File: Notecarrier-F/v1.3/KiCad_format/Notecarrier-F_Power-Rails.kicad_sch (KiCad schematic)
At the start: 31 parts, among them U3 TPS63020DSJR, U7 MAX17225ELT+, U8 TPS62748YFPT, U9 AP2139AK-3.3TRG1

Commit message: kicad_validation: make the BOM and placement gates actually gate
Two of the three proof gates could not fail on the thing they claimed to check.

BOM: the MPN comparison was guarded on `k["mpn"]` being non-empty, so a released
BOM naming a part and a KiCad symbol carrying no MPN at all compared equal and
reported "PASS - BOM matches exactly". Missing data was being read as agreement.
Value and MPN were also chained with elif, so an MPN mismatch was hidden behind
a value mismatch on the same refdes. Both fixed, and a blank KiCad MPN now fails
whenever the shipped BOM has one.

That immediately caught real data loss: C33 and C34, added to Notecarrier-F
earlier on this branch, had no MPN. Set to CC0603KRX5R8BB105 / Yageo per
BOM-3000-653-002. J11 is the only remaining blank and it is DNP, so excluded.

Placement: the gate computed position residuals and then omitted them from the
verdict, so a footprint could move anywhere and still pass - and
allowed_position_outliers was configured for X and XS but read by no code.

Rather than bless the residuals with a hand-kept table, each part's expected
residual is now predicted from its own pad bounding box, since the assembly file
references the body centre while KiCad measures from the footprint origin. That
explains almost everything outright: Notecarrier-XI's P1/P2 sit 19.05mm out
because their footprint - named "1X16" - has its origin on pad 1 of a 38.1mm
header, which is exactly half its length.

What the prediction cannot explain must be listed in a committed
placement-baseline.yaml, so it is reviewed once and then frozen against drift.
The 12 entries across five boards are all 0.3-0.7mm on JST connectors with a
plastic shroud wider than their pads, and on diodes whose large tab pad pulls
the pad bounding box off the package centre. allowed_position_outliers is gone,
superseded by that file.

Verified by nudging one Notecarrier-XM footprint 1mm: the gate now fails it.
All five configured boards pass with their baselines 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
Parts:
- C33, C34: MPN (none) -> CC0603KRX5R8BB105; Manufacturer (none) -> Yageo
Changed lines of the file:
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@@
+			)
+		)
+		(property "MPN" "CC0603KRX5R8BB105"
+			(at 203.2 33.02 0)
+			(effects
+				(font
+					(size 1.27 1.27)
+				)
+				(hide yes)
+			)
+		)
+		(property "Manufacturer" "Yageo"
+			(at 203.2 33.02 0)
+			(effects
+				(font
+					(size 1.27 1.27)
+				)
+				(hide yes)
 			)
 		)
@@
 			)
 		)
+		(property "MPN" "CC0603KRX5R8BB105"
+			(at 226.06 33.02 0)
+			(effects
+				(font
+					(size 1.27 1.27)
+				)
+				(hide yes)
+			)
+		)
+		(property "Manufacturer" "Yageo"
+			(at 226.06 33.02 0)
+			(effects
+				(font
+					(size 1.27 1.27)
+				)
+				(hide yes)
+			)
+		)

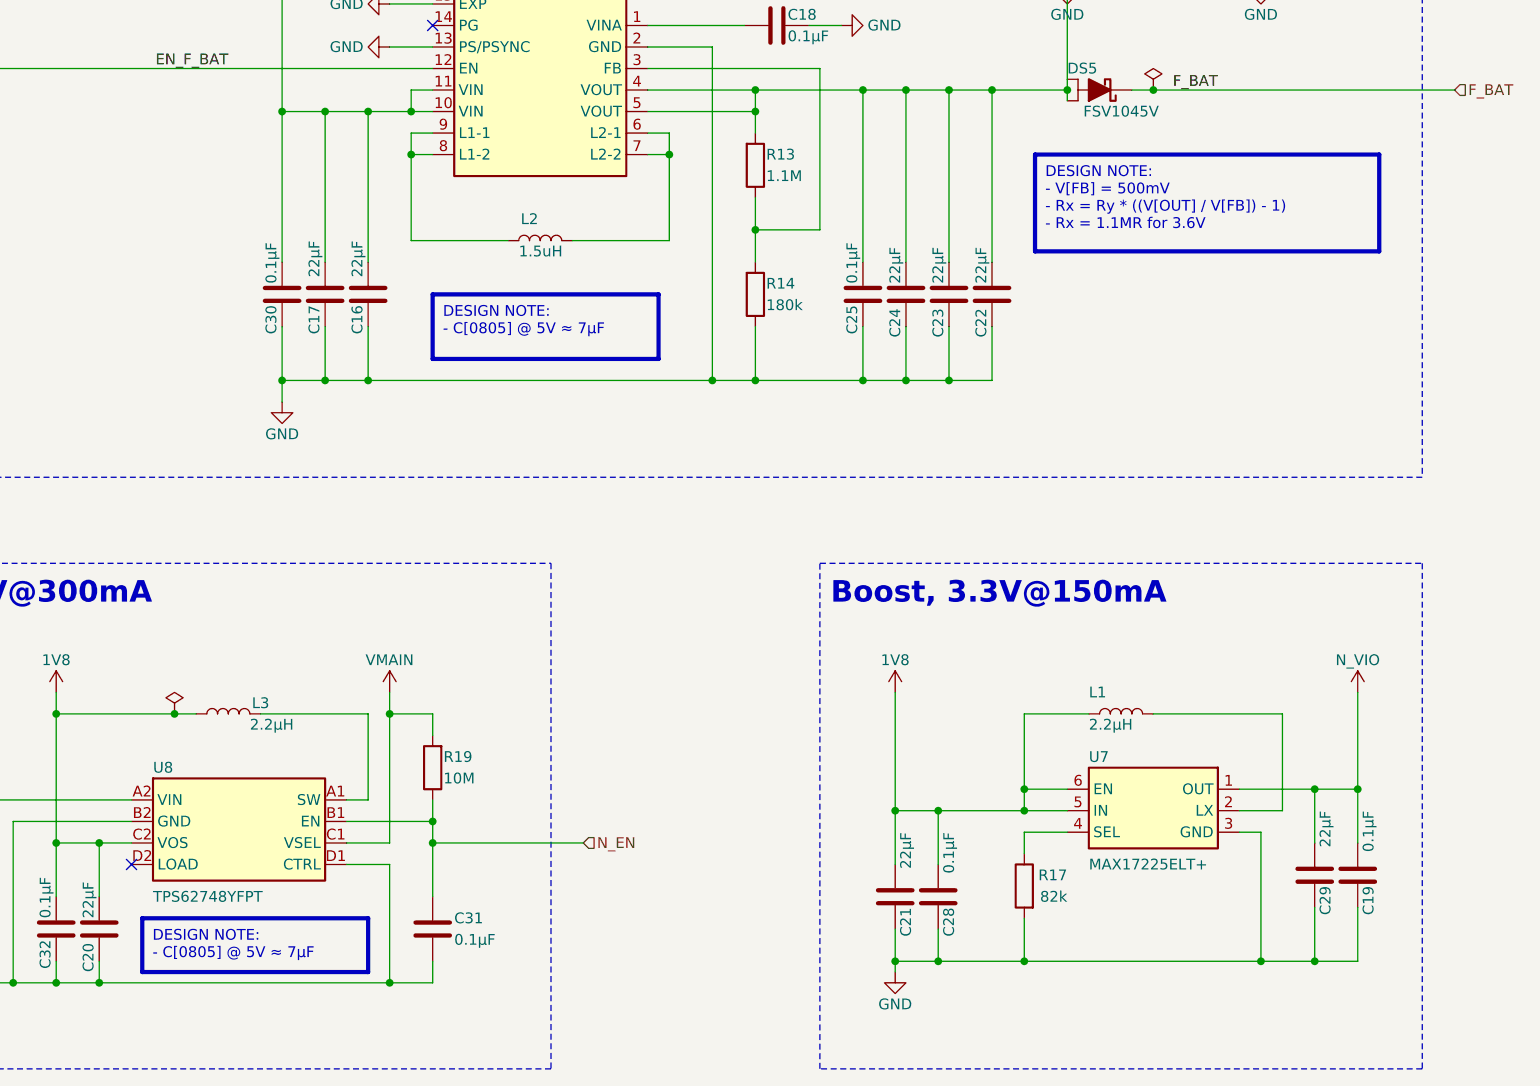
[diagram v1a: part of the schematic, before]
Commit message: Notecarrier-F: convert its design-note text_boxes too
The first conversion pass scoped by red-frame rectangles and missed
Notecarrier-F: its 16 notes have no separate frame - the text_box itself draws
a 0.5mm red border - so they were entirely invisible on the published pages,
frames included. Same conversion as 25a2d84, with two additions the F notes
forced:

- KiCad's hidden PDF text layer mangles special glyphs (broken ToUnicode maps
  for u/~/ohm produce mojibake) and F's notes are full of them, so exact
  word-matching is unattainable. Notes whose visual line count matches their
  source line count need no wrap-freezing at all and are kept verbatim, guarded
  by a per-line ASCII similarity check; only genuinely wrapped notes use the
  strict word-level path, and F's wrapped notes are clean of special glyphs.
  The converter also now rebuilds output from SOURCE words - the PDF only
  supplies break positions - so KiCad markup like R_{iset} stays markup in the
  file instead of being replaced by its rendered form.

- The F author gave these notes an explicit black font color. Black is what
  KiCad plots either way, but explicit black is invisible on a dark-theme
  viewer. The 16 notes now carry no explicit color, like every other board's
  notes: KiCad plots its default dark blue, kicanvas its theme color. This is
  the one deliberate visual change - note text black -> dark blue in KiCad -
  and it makes F consistent with the other five boards.

Netlist byte-equal before and after; kicanvas renders all four modified sheets
with the notes visible and the subscript markup intact.

Co-Authored-By: Claude Fable 5 <noreply@anthropic.com>
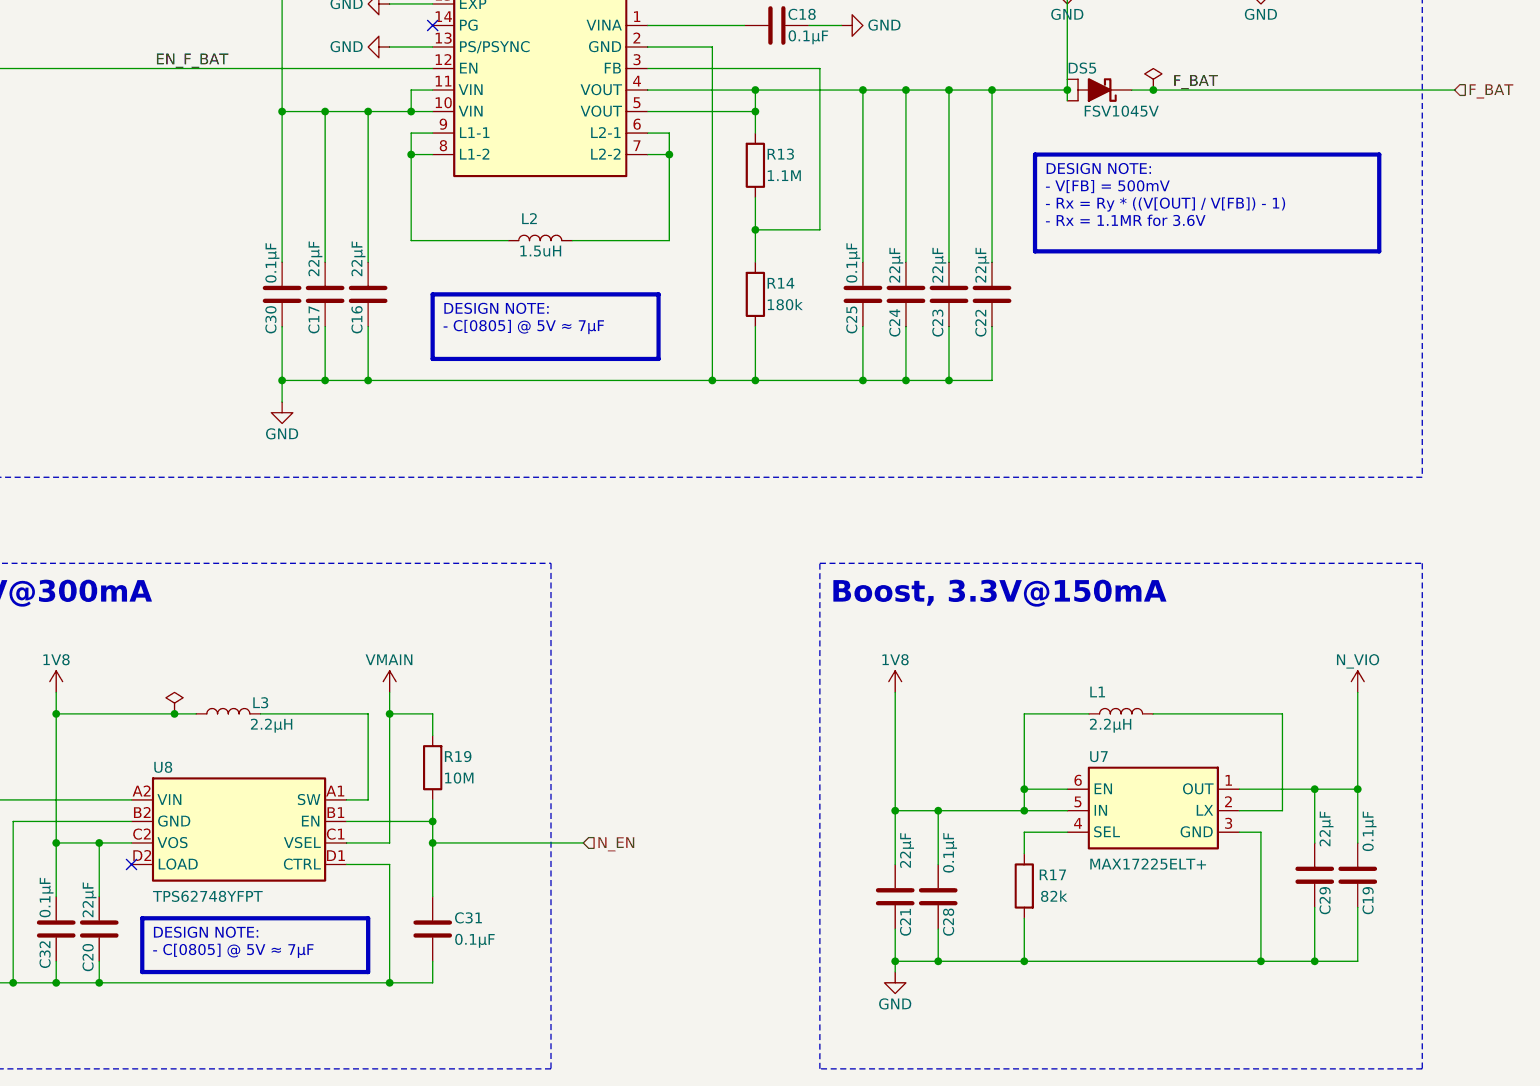
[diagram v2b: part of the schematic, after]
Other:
- note added: "DESIGN NOTE: - C[0805] @ 5V ≈ 7µF"
- note added: "DESIGN NOTE: - V[FB] = 500mV - Rx = Ry * ((V[OUT] / V[FB]) - 1) - Rx = 1.1MR for 3.6V"
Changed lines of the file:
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@@
 		)
 	)
-	(text_box "DESIGN NOTE:\n- C[0805] @ 5V ≈ 7µF"
-		(exclude_from_sim no)
-		(at 128.27 73.66 0)
-		(size 26.67 7.62)
-		(margins 1.2025 1.2025 1.2025 1.2025)
+	(rectangle
+		(start 128.27 73.66)
+		(end 154.94 81.28)
 		(stroke
 			(width 0.5)
@@
 			(type none)
 		)
+	)
+	(text "DESIGN NOTE:\n- C[0805] @ 5V ≈ 7µF"
+		(exclude_from_sim no)
+		(at 129.472 74.8625 0)
 		(effects
 			(font
 				(size 1.27 1.27)
-				(color 0 0 0 1)
 			)
 			(justify left top)
 		)
 	)
-	(text_box "DESIGN NOTE:\n- C[0805] @ 5V ≈ 7µF"
-		(exclude_from_sim no)
-		(at 93.98 147.32 0)
-		(size 26.67 6.35)
-		(margins 1.2025 1.2025 1.2025 1.2025)
+	(rectangle
+		(start 93.98 147.32)
+		(end 120.65 153.67)
 		(stroke
 			(width 0.5)
@@
 			(type none)
 		)
+	)
+	(text "DESIGN NOTE:\n- C[0805] @ 5V ≈ 7µF"
+		(exclude_from_sim no)
+		(at 95.1825 148.522 0)
 		(effects
 			(font
 				(size 1.27 1.27)
-				(color 0 0 0 1)
 			)
 			(justify left top)
 		)
 	)
-	(text_box "DESIGN NOTE:\n- V[FB] = 500mV\n- Rx = Ry * ((V[OUT] / V[FB]) - 1)\n- Rx = 1.1MR for 3.6V"
-		(exclude_from_sim no)
-		(at 199.39 57.15 0)
-		(size 40.64 11.43)
-		(margins 1.2025 1.2025 1.2025 1.2025)
+	(rectangle
+		(start 199.39 57.15)
+		(end 240.03 68.58)
 		(stroke
 			(width 0.5)
@@
 			(type none)
 		)
+	)
+	(text "DESIGN NOTE:\n- V[FB] = 500mV\n- Rx = Ry * ((V[OUT] / V[FB]) - 1)\n- Rx = 1.1MR for 3.6V"
+		(exclude_from_sim no)
+		(at 200.592 58.3525 0)
 		(effects
 			(font
 				(size 1.27 1.27)
-				(color 0 0 0 1)
 			)
 			(justify left top)
